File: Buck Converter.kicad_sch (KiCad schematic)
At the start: 30 parts, among them J1 Conn_01x02, J2 Conn_01x02, SW1 SW_SPST, U1 LT3684xMSE

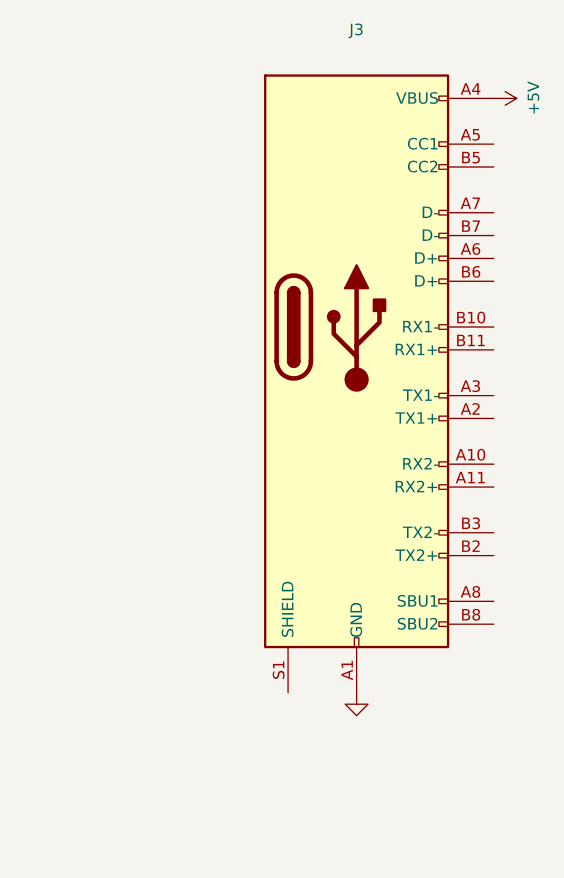
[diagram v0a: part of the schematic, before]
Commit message: Minor Tweaks
Updated PCB with the following recommendations:

1. Clean up the ERC and DRC issues.  The schematic has the USB connector without it being on the PCB; there's an unmade connection on TP6, and the silkscreen needs to be cleaned up.
2. Move the switch inward from the edge of the board.  The holes are close enough to the edge to cause some grief.
3. Move R5 a bit south.  It's an easy fix to clear up the path for VCC to get from J1.1 to U1.4.  Also to make way for:
3. Move C1 closer to the IC.  The bypass caps should be as close as possible to their associated ICs.
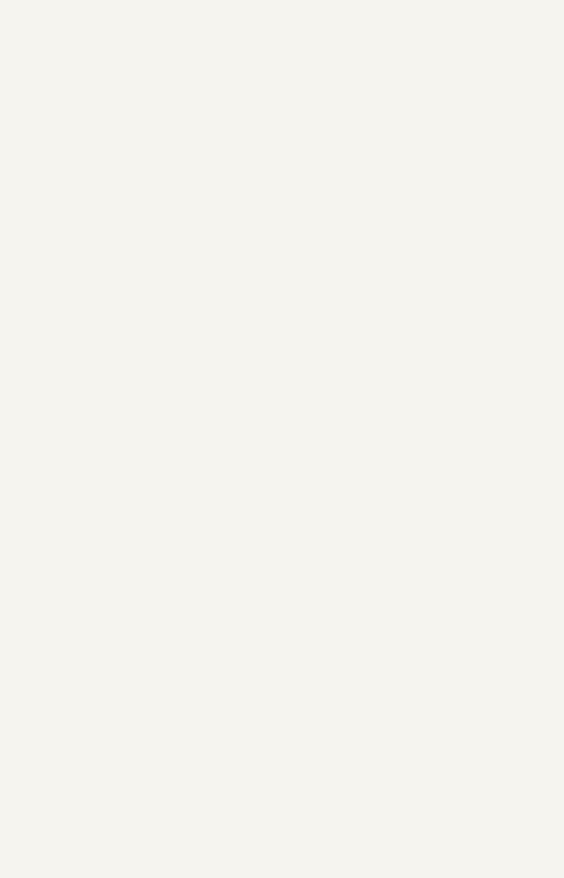
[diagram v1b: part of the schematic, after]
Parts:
- removed J3: (no value), symbol Connector:USB_C_Receptacle
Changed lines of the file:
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@@
-    (pin "1")
-  )
-  (symbol (lib_id "power:+5V") (at 262.89 41.91 270) (unit 1)
-    (in_bom yes) (on_board yes)
-    (property "Reference" "#PWR0101" (id 0) (at 259.08 41.91 0)
-      (effects (font (size 1.27 1.27)) hide)
-    )
-    (property "Value" "+5V" (id 1) (at 267.335 40.005 0)
-      (effects (font (size 1.27 1.27)) (justify left))
-    )
-    (property "Footprint" "" (id 2) (at 262.89 41.91 0)
-      (effects (font (size 1.27 1.27)) hide)
-    )
-    (property "Datasheet" "" (id 3) (at 262.89 41.91 0)
-      (effects (font (size 1.27 1.27)) hide)
-    )
     (pin "1")
   )
@@
     )
     (pin "1")
-  )
-  (symbol (lib_id "Connector:USB_C_Receptacle") (at 247.65 67.31 0) (unit 1)
-    (in_bom yes) (on_board yes) (fields_autoplaced)
-    (property "Reference" "J3" (id 0) (at 247.65 34.29 0))
-    (property "Value" "" (id 1) (at 247.65 36.83 0))
-    (property "Footprint" "" (id 2) (at 251.46 67.31 0)
-      (effects (font (size 1.27 1.27)) hide)
-    )
-    (property "Datasheet" "https://www.usb.org/sites/default/files/documents/usb_type-c.zip" (id 3) (at 251.46 67.31 0)
-      (effects (font (size 1.27 1.27)) hide)
-    )
-    (pin "A1")
-    (pin "A10")
-    (pin "A11")
-    (pin "A12")
-    (pin "A2")
-    (pin "A3")
-    (pin "A4")
-    (pin "A5")
-    (pin "A6")
-    (pin "A7")
-    (pin "A8")
-    (pin "A9")
-    (pin "B1")
-    (pin "B10")
-    (pin "B11")
-    (pin "B12")
-    (pin "B2")
-    (pin "B3")
-    (pin "B4")
-    (pin "B5")
-    (pin "B6")
-    (pin "B7")
-    (pin "B8")
-    (pin "B9")
-    (pin "S1")
   )
   (symbol (lib_id "Device:C_Small") (at 105.41 124.46 0) (unit 1)
@@
     (pin "9")
   )
-  (symbol (lib_id "power:GND") (at 247.65 107.95 0) (unit 1)
-    (in_bom yes) (on_board yes)
-    (property "Reference" "#PWR0102" (id 0) (at 247.65 114.3 0)
-      (effects (font (size 1.27 1.27)) hide)
-    )
-    (property "Value" "GND" (id 1) (at 251.46 109.22 0)
-      (effects (font (size 1.27 1.27)) hide)
-    )
-    (property "Footprint" "" (id 2) (at 247.65 107.95 0)
-      (effects (font (size 1.27 1.27)) hide)
-    )
-    (property "Datasheet" "" (id 3) (at 247.65 107.95 0)
-      (effects (font (size 1.27 1.27)) hide)
-    )
-    (pin "1")
-  )
   (symbol (lib_id "Connector:TestPoint") (at 134.62 125.73 90) (unit 1)
     (in_bom yes) (on_board yes)
@@
       (reference "#PWR014") (unit 1) (value "GND") (footprint "")
     )
-    (path "/0da8f855-96b9-46b1-9d50-dc47ff61091f"
-      (reference "#PWR0101") (unit 1) (value "+5V") (footprint "")
-    )
-    (path "/710de379-d14b-4d9b-8e5a-43608abe725a"
-      (reference "#PWR0102") (unit 1) (value "GND") (footprint "")
-    )
     (path "/7306d213-dfff-4d2e-909b-5a6e30b34d0b"
       (reference "C1") (unit 1) (value "2.2uF") (footprint "Capacitor_SMD:C_0603_1608Metric_Pad1.08x0.95mm_HandSolder")
@@
       (reference "J2") (unit 1) (value "Conn_01x02") (footprint "Connector_Phoenix_MSTB:PhoenixContact_MSTBVA_2,5_2-G_1x02_P5.00mm_Vertical")
     )
-    (path "/3c60029a-7bb2-4ac9-8034-42351038f32f"
-      (reference "J3") (unit 1) (value "USB_C_Receptacle") (footprint "Connector_USB:USB_C_Receptacle_Amphenol_12401548E4-2A")
-    )
     (path "/282aa89d-2515-4eb9-9877-8f65e7e848ba"
